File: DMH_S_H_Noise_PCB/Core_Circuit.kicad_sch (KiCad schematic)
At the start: 61 parts, among them Q1 BC548, Q2 MMBFJ113, Q3 BC548, SW1 SW_Push, U1 TL074, U2 TL072, U3 TL074

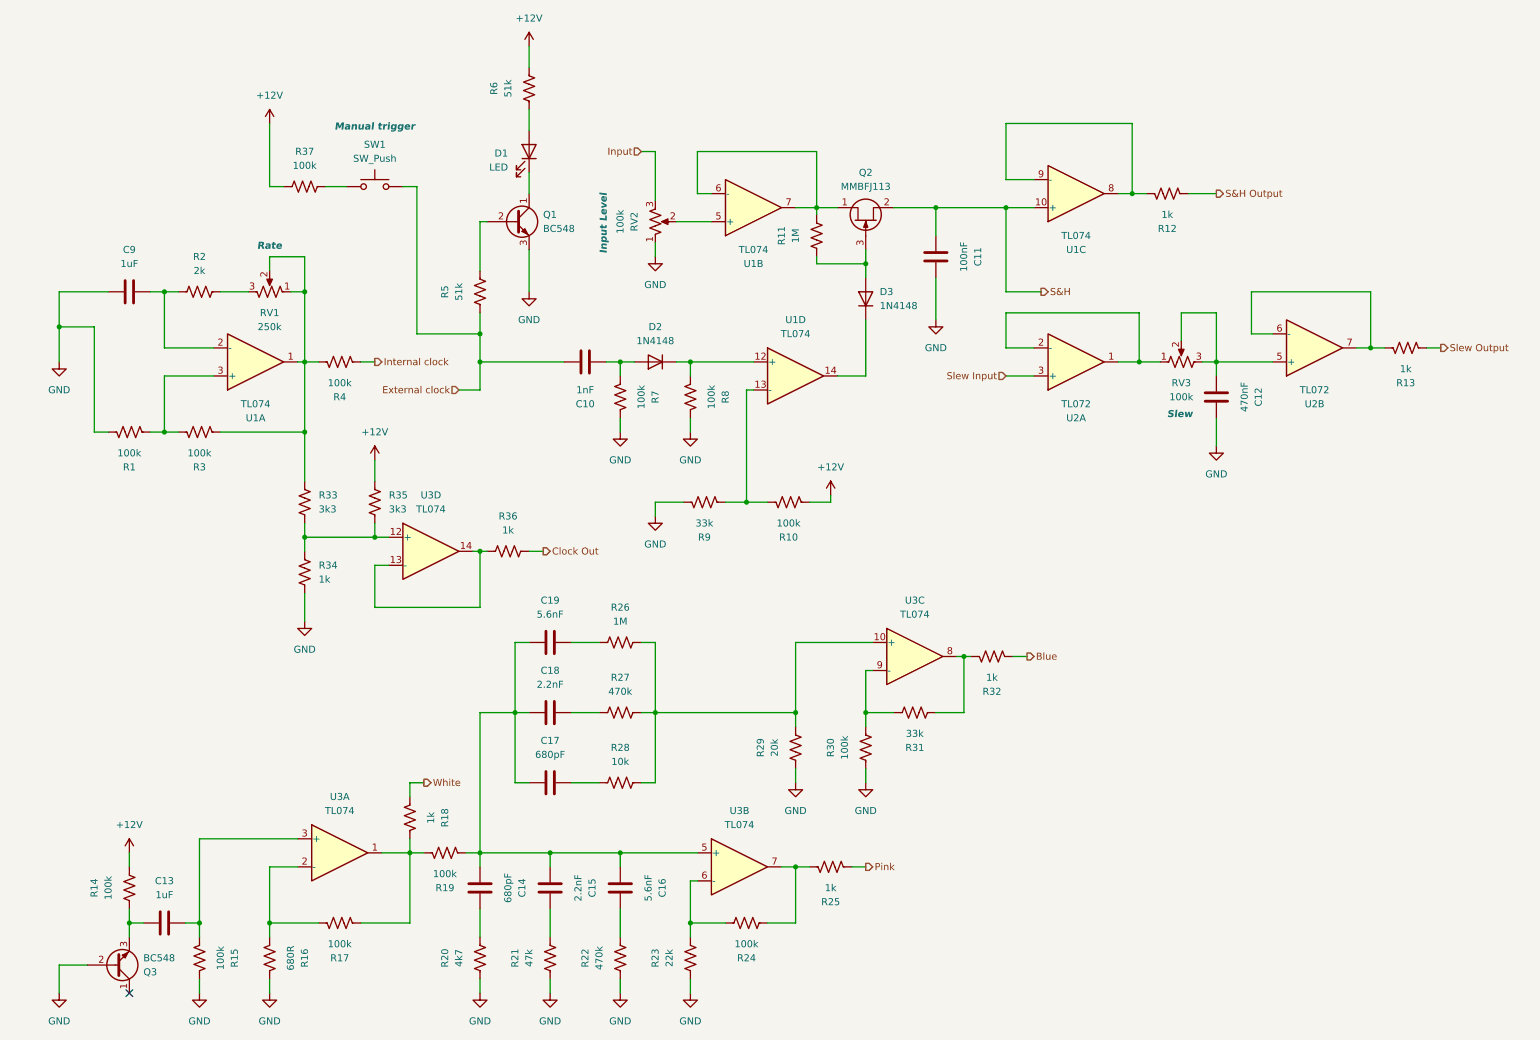
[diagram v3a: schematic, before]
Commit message: Corrections during breadboard assembly
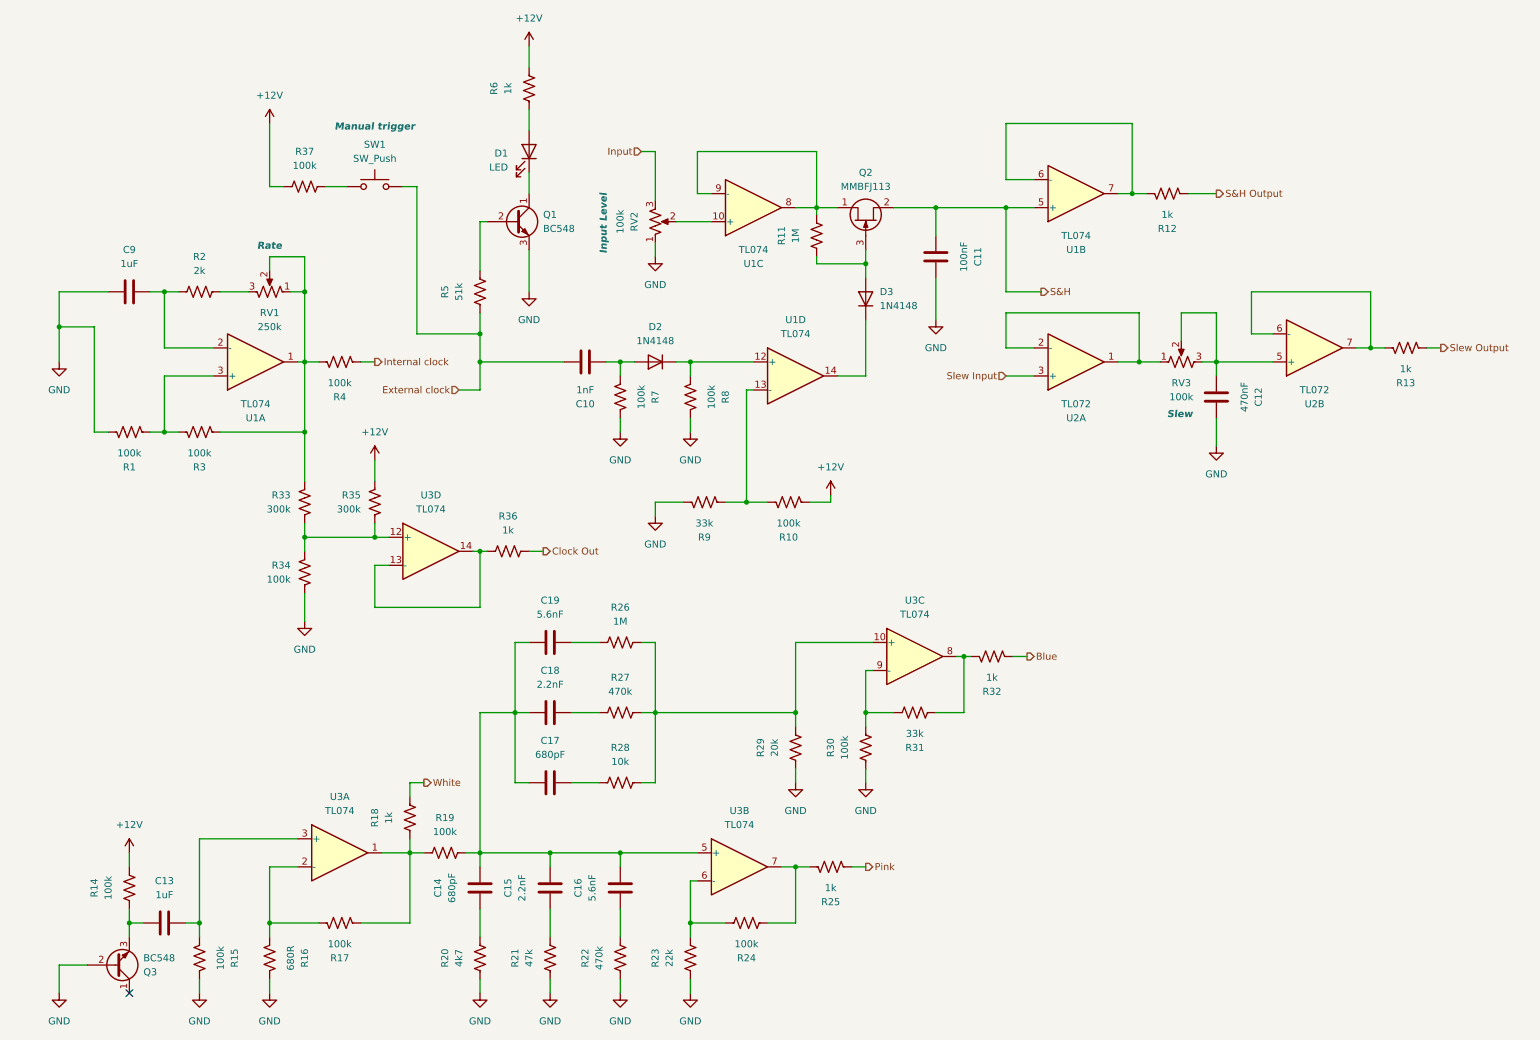
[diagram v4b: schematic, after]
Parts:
- R33, R35: value 3k3 -> 300k
- R34: value 1k -> 100k
- R6: value 51k -> 1k
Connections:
- net S&H: now also U1.5 (+); no longer U1.10 (+)
- net at RV2.2: now also U1.10 (+); no longer U1.5 (+)
- net at Q2.1 (D), R11.1: now also U1.8, U1.9 (-); no longer U1.6 (-), U1.7
- new net: R12.2, U1.6 (-), U1.7
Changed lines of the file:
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@@
 	)
 	(junction
+		(at 76.2 107.95)
+		(diameter 0)
+		(color 0 0 0 0)
+	)
+	(junction
 		(at 63.5 76.2)
 		(diameter 0)
@@
 	)
 	(junction
-		(at 76.2 107.95)
-		(diameter 0)
-		(color 0 0 0 0)
-	)
-	(junction
 		(at 82.55 165.1)
 		(diameter 0)
@@
 	(wire
 		(pts
+			(xy 63.5 107.95) (xy 76.2 107.95)
+		)
+		(stroke
+			(width 0)
+			(type default)
+		)
+	)
+	(wire
+		(pts
 			(xy 63.5 76.2) (xy 66.04 76.2)
 		)
@@
 	(wire
 		(pts
-			(xy 76.2 107.95) (xy 78.74 107.95)
-		)
-		(stroke
-			(width 0)
-			(type default)
-		)
-	)
-	(wire
-		(pts
 			(xy 111.76 152.4) (xy 116.84 152.4)
 		)
@@
 	(wire
 		(pts
+			(xy 76.2 107.95) (xy 78.74 107.95)
+		)
+		(stroke
+			(width 0)
+			(type default)
+		)
+	)
+	(wire
+		(pts
 			(xy 222.25 67.31) (xy 228.6 67.31)
 		)
@@
 	(wire
 		(pts
-			(xy 76.2 107.95) (xy 63.5 107.95)
-		)
-		(stroke
-			(width 0)
-			(type default)
-		)
-	)
-	(wire
-		(pts
 			(xy 133.35 86.36) (xy 133.35 88.9)
 		)
@@
 		(at 144.78 48.26 0)
 		(mirror x)
-		(unit 2)
+		(unit 3)
 		(exclude_from_sim no)
 		(in_bom yes)
@@
 			)
 		)
+		(property "Function" ""
+			(at 144.78 48.26 0)
+			(effects
+				(font
+					(size 1.27 1.27)
+				)
+			)
+		)
 		(pin "14"
 		)
@@
 				(path "/58f4306d-5387-4983-bb08-41a2313fd315/7ad2d702-dfb7-4d49-a82d-34430dd5948f"
 					(reference "U1")
-					(unit 2)
+					(unit 3)
 				)
 			)
@@
 		(lib_id "Device:R_US")
 		(at 63.5 101.6 0)
+		(mirror y)
 		(unit 1)
 		(exclude_from_sim no)
@@
 		(on_board yes)
 		(dnp no)
-		(fields_autoplaced yes)
 		(property "Reference" "R33"
-			(at 66.04 100.3299 0)
+			(at 60.96 100.3299 0)
 			(effects
 				(font
@@
 			)
 		)
-		(property "Value" "3k3"
-			(at 66.04 102.8699 0)
+		(property "Value" "300k"
+			(at 60.96 102.8699 0)
 			(effects
 				(font
@@
 		)
 		(property "Footprint" "Resistor_THT:R_Axial_DIN0207_L6.3mm_D2.5mm_P7.62mm_Horizontal"
-			(at 64.516 101.854 90)
+			(at 62.484 101.854 90)
 			(effects
 				(font
@@
 			)
 		)
-		(property "Value" "51k"
+		(property "Value" "1k"
 			(at 100.33 26.67 90)
 			(effects
@@
 			)
 		)
+		(property "Function" ""
+			(at 54.61 76.2 0)
+			(effects
+				(font
+					(size 1.27 1.27)
+				)
+			)
+		)
 		(pin "14"
 		)
@@
 		(lib_id "Device:C")
 		(at 107.95 171.45 0)
-		(mirror y)
 		(unit 1)
 		(exclude_from_sim no)
@@
 		(dnp no)
 		(property "Reference" "C15"
-			(at 115.57 171.45 90)
+			(at 100.33 171.45 90)
 			(effects
 				(font
@@
 		)
 		(property "Value" "2.2nF"
-			(at 113.03 171.45 90)
+			(at 102.87 171.45 90)
 			(effects
 				(font
@@
 		)
 		(property "Footprint" "Capacitor_THT:C_Disc_D4.3mm_W1.9mm_P5.00mm"
-			(at 106.9848 175.26 0)
+			(at 108.9152 175.26 0)
 			(effects
 				(font
@@
 			)
 		)
+		(property "Function" ""
+			(at 152.4 78.74 0)
+			(effects
+				(font
+					(size 1.27 1.27)
+				)
+			)
+		)
 		(pin "14"
 		)
@@
 		(lib_id "Device:R_US")
 		(at 82.55 158.75 0)
-		(mirror y)
 		(unit 1)
 		(exclude_from_sim no)
@@
 		(dnp no)
 		(property "Reference" "R18"
-			(at 88.9 158.75 90)
+			(at 76.2 158.75 90)
 			(effects
 				(font
@@
 		)
 		(property "Value" "1k"
-			(at 86.36 158.75 90)
+			(at 78.74 158.75 90)
 			(effects
 				(font
@@
 		)
 		(property "Footprint" "Resistor_THT:R_Axial_DIN0207_L6.3mm_D2.5mm_P7.62mm_Horizontal"
-			(at 81.534 159.004 90)
+			(at 83.566 159.004 90)
 			(effects
 				(font
@@
 		(lib_id "Device:R_US")
 		(at 76.2 101.6 0)
+		(mirror y)
 		(unit 1)
 		(exclude_from_sim no)
@@
 		(on_board yes)
 		(dnp no)
-		(fields_autoplaced yes)
 		(property "Reference" "R35"
-			(at 78.74 100.3299 0)
+			(at 73.66 100.3299 0)
 			(effects
 				(font
@@
 			)
 		)
-		(property "Value" "3k3"
-			(at 78.74 102.8699 0)
+		(property "Value" "300k"
+			(at 73.66 102.8699 0)
 			(effects
 				(font
@@
 		)
 		(property "Footprint" "Resistor_THT:R_Axial_DIN0207_L6.3mm_D2.5mm_P7.62mm_Horizontal"
-			(at 77.216 101.854 90)
+			(at 75.184 101.854 90)
 			(effects
 				(font
@@
 		(lib_id "Device:R_US")
 		(at 88.9 165.1 270)
-		(mirror x)
 		(unit 1)
 		(exclude_from_sim no)
@@
 		(dnp no)
 		(property "Reference" "R19"
-			(at 88.9 171.45 90)
+			(at 88.9 158.75 90)
 			(effects
 				(font
@@
 		)
 		(property "Value" "100k"
-			(at 88.9 168.91 90)
+			(at 88.9 161.29 90)
 			(effects
 				(font
@@
 		)
 		(property "Footprint" "Resistor_THT:R_Axial_DIN0207_L6.3mm_D2.5mm_P7.62mm_Horizontal"
-			(at 88.646 164.084 90)
+			(at 88.646 166.116 90)
 			(effects
 				(font
@@
 		(at 203.2 45.72 0)
 		(mirror x)
-		(unit 3)
+		(unit 2)
 		(exclude_from_sim no)
 		(in_bom yes)
@@
 			)
 		)
+		(property "Function" ""
+			(at 203.2 45.72 0)
+			(effects
+				(font
+					(size 1.27 1.27)
+				)
+			)
+		)
 		(pin "14"
 		)
@@
 				(path "/58f4306d-5387-4983-bb08-41a2313fd315/7ad2d702-dfb7-4d49-a82d-34430dd5948f"
 					(reference "U1")
-					(unit 3)
+					(unit 2)
 				)
 			)
@@
 		(lib_id "Device:C")
 		(at 95.25 171.45 0)
-		(mirror y)
 		(unit 1)
 		(exclude_from_sim no)
@@
 		(dnp no)
 		(property "Reference" "C14"
-			(at 102.87 171.45 90)
+			(at 87.63 171.45 90)
 			(effects
 				(font
@@
 		)
 		(property "Value" "680pF"
-			(at 100.33 171.45 90)
+			(at 90.17 171.45 90)
 			(effects
 				(font
@@
 		)
 		(property "Footprint" "Capacitor_THT:C_Disc_D4.3mm_W1.9mm_P5.00mm"
-			(at 94.2848 175.26 0)
+			(at 96.2152 175.26 0)
 			(effects
 				(font
@@
 		(lib_id "Device:C")
 		(at 120.65 171.45 0)
-		(mirror y)
 		(unit 1)
 		(exclude_from_sim no)
@@
 		(dnp no)
 		(property "Reference" "C16"
-			(at 128.27 171.45 90)
+			(at 113.03 171.45 90)
 			(effects
 				(font
@@
 		)
 		(property "Value" "5.6nF"
-			(at 125.73 171.45 90)
+			(at 115.57 171.45 90)
 			(effects
 				(font
@@
 		)
 		(property "Footprint" "Capacitor_THT:C_Disc_D4.3mm_W1.9mm_P5.00mm"
-			(at 119.6848 175.26 0)
+			(at 121.6152 175.26 0)
 			(effects
 				(font
@@
 		(lib_id "Device:R_US")
 		(at 63.5 114.3 0)
+		(mirror y)
 		(unit 1)
 		(exclude_from_sim no)
@@
 		(on_board yes)
 		(dnp no)
-		(fields_autoplaced yes)
 		(property "Reference" "R34"
-			(at 66.04 113.0299 0)
+			(at 60.96 113.0299 0)
 			(effects
 				(font
@@
 			)
 		)
-		(property "Value" "1k"
-			(at 66.04 115.5699 0)
+		(property "Value" "100k"
+			(at 60.96 115.5699 0)
 			(effects
 				(font
@@
 		)
 		(property "Footprint" "Resistor_THT:R_Axial_DIN0207_L6.3mm_D2.5mm_P7.62mm_Horizontal"
-			(at 64.516 114.554 90)
+			(at 62.484 114.554 90)
 			(effects
 				(font

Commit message: Updated resistor values after test
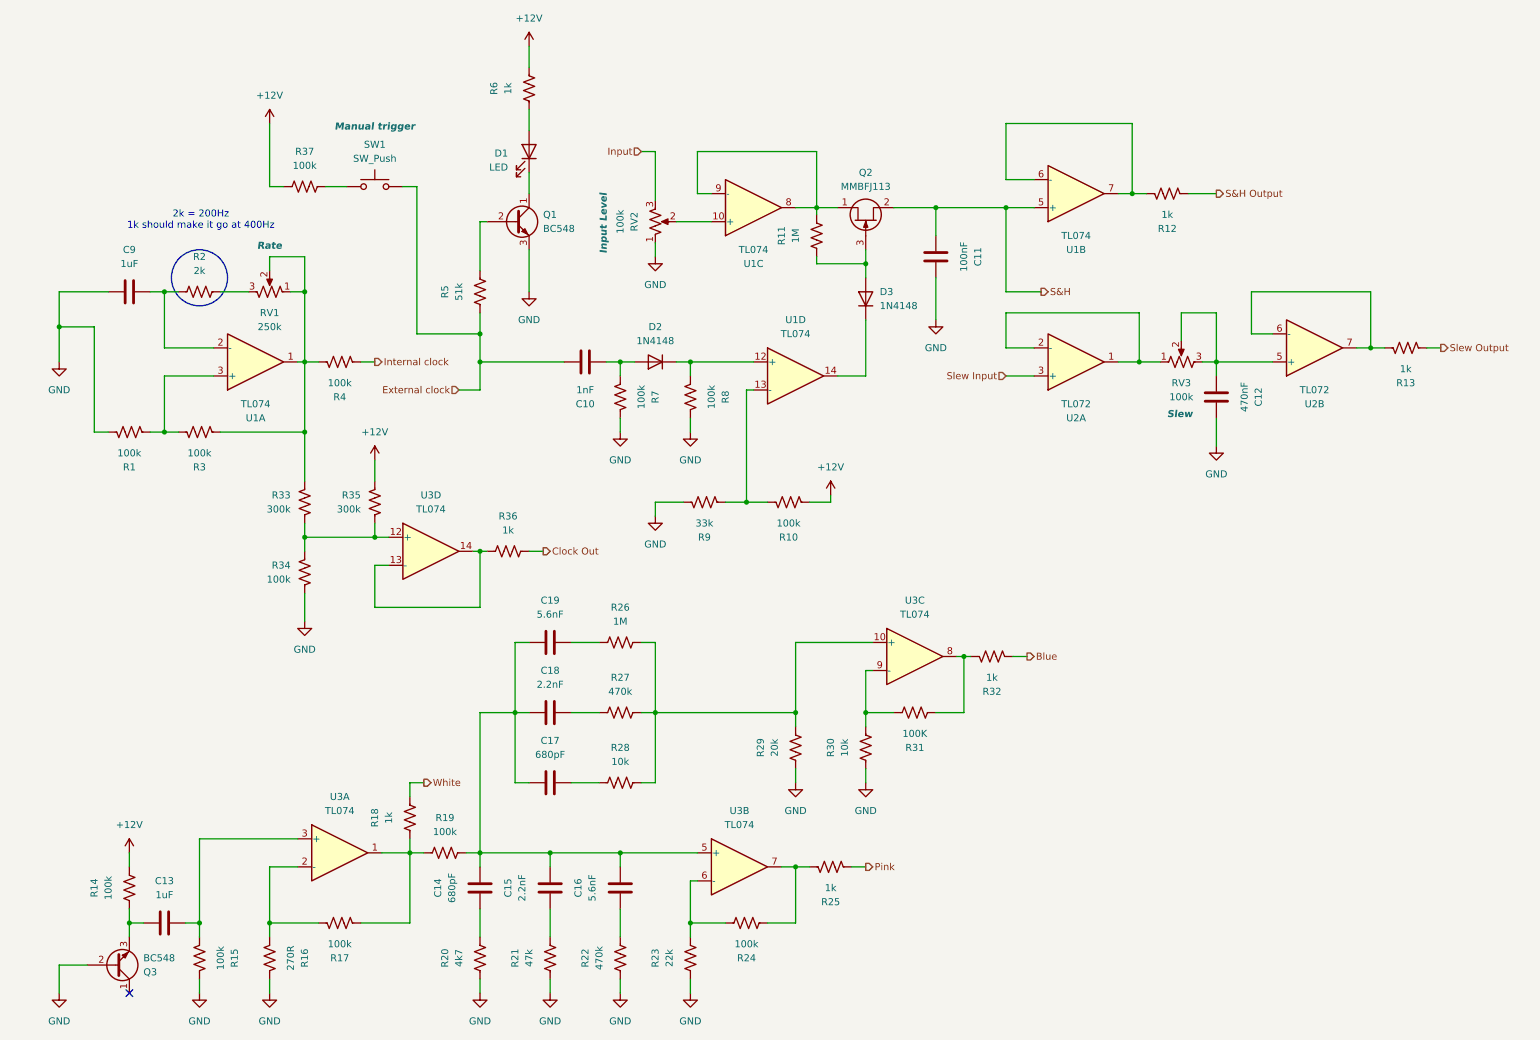
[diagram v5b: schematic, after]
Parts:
- R16: value 680R -> 270R
- R30: value 100k -> 10k
- R31: value 33k -> 100K
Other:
- note added: "2k = 200Hz 1k should make it go at 400Hz"
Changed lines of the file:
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@@
 		)
 	)
+	(circle
+		(center 44.45 60.96)
+		(radius 5.08)
+		(stroke
+			(width 0)
+			(type default)
+		)
+		(fill
+			(type none)
+		)
+	)
+	(text "2k = 200Hz\n1k should make it go at 400Hz"
+		(exclude_from_sim no)
+		(at 44.704 50.546 0)
+		(effects
+			(font
+				(size 1.27 1.27)
+			)
+		)
+	)
 	(hierarchical_label "Internal clock"
 		(shape output)
@@
 			)
 		)
-		(property "Value" "680R"
+		(property "Value" "270R"
 			(at 60.96 184.15 90)
 			(effects
@@
 			)
 		)
-		(property "Value" "100k"
+		(property "Value" "10k"
 			(at 161.29 146.05 90)
 			(effects
@@
 			)
 		)
-		(property "Value" "33k"
+		(property "Value" "100K"
 			(at 173.99 143.51 90)
 			(effects

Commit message: Update Core_Circuit.kicad_sch
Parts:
- removed R35: 300k, Resistor_THT:R_Axial_DIN0207_L6.3mm_D2.5mm_P7.62mm_Horizontal, symbol Device:R_US
- added D6: ZPDxx, Diode_THT:D_DO-35_SOD27_P10.16mm_Horizontal, symbol Diode:ZPDxx
- C12: value 470nF -> 1uF
- R33: value 300k -> 1k
- R36: value 1k -> 100k
- R6: value 1k -> 2k
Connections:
- net External clock: now also R33.1, R34.2; no longer C10.2, R5.2, SW1.2
- net GND: now also R34.1, D6.2 (A); no longer R34.2
- net at R3.1, R4.2, RV1.1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: no longer R33.1
- net at R33.2, U3.12 (+): now also D6.1 (K); no longer R34.1
- net at R36.1, U3.14: no longer U3.13 (-)
- net at R10.2, R9.1, U1.13 (-): now also U3.13 (-)
- net Clock Out: no longer names the net of R36.2
- net Clock Out: now also C10.2, R5.2, SW1.2
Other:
- moved on the sheet: R36, U3D

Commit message: Finished schematic
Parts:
- removed D6: ZPDxx, Diode_THT:D_DO-35_SOD27_P10.16mm_Horizontal, symbol Diode:ZPDxx
- removed R33: 1k, Resistor_THT:R_Axial_DIN0207_L6.3mm_D2.5mm_P7.62mm_Horizontal, symbol Device:R_US
- added R35: 20k, Resistor_THT:R_Axial_DIN0207_L6.3mm_D2.5mm_P7.62mm_Horizontal, symbol Device:R_US
- added R38: 100k, Resistor_THT:R_Axial_DIN0207_L6.3mm_D2.5mm_P7.62mm_Horizontal, symbol Device:R_US
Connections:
- net External clock is gone; now on an unnamed net: R34.2
- net Internal clock is gone; now on an unnamed net: R4.1
- net +12V: now also R38.1
- net GND: now also R35.2
- net at U3.12 (+): now also SW1.2
- net at C10.2, R36.2, R5.2: no longer SW1.2
- net at R10.2, R9.1, U1.13 (-): no longer U3.13 (-)
- net Internal Clock: now reaches R3.1, RV1.1, RV1.2, U1.1
- net Internal Clock: no longer R4.2
- new net: R35.1, R38.2, U3.13 (-)
- new net External Clock: R4.2
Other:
- moved on the sheet: R34, U1A
